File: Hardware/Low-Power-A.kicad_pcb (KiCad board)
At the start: 2 copper layers, 65.4 x 41.3 mm, 27 parts, among them J1 USB_A, J2 01x02, Q1 BC557, Q2 BC547, Q3 BC557, Q4 BC547, Q5 BC547, U1 Arduino_Pro_Micro, U2 VS1838B

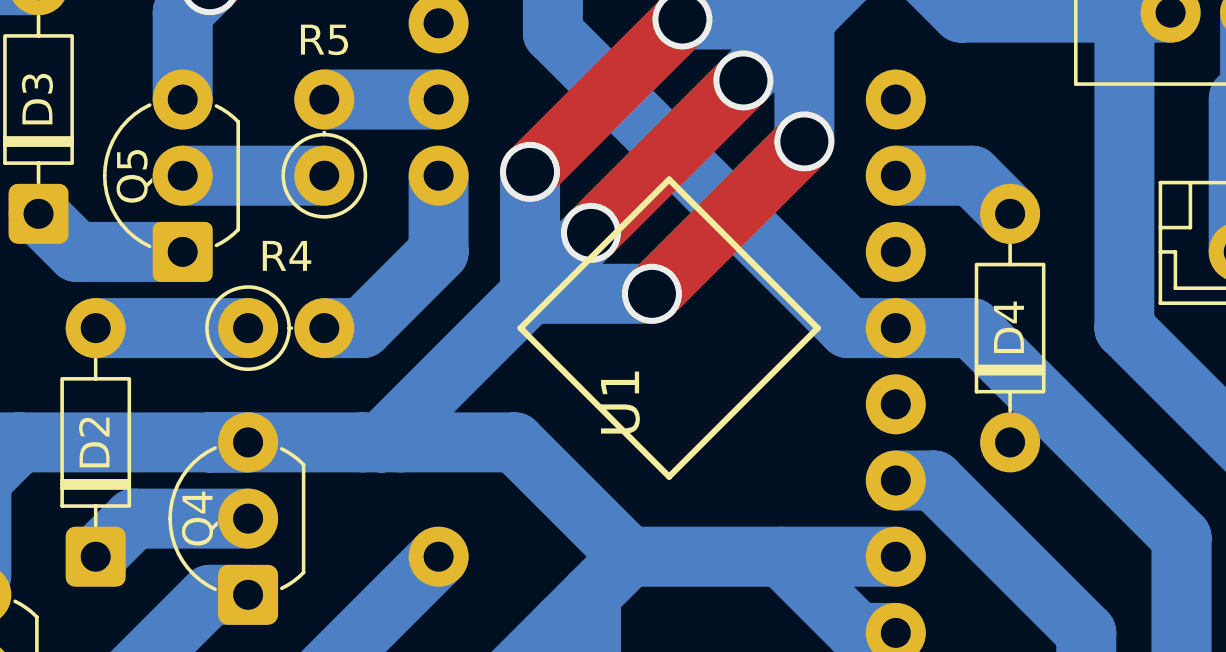
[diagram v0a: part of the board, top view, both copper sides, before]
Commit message: Adding Low-Power-B version schematics & PCB
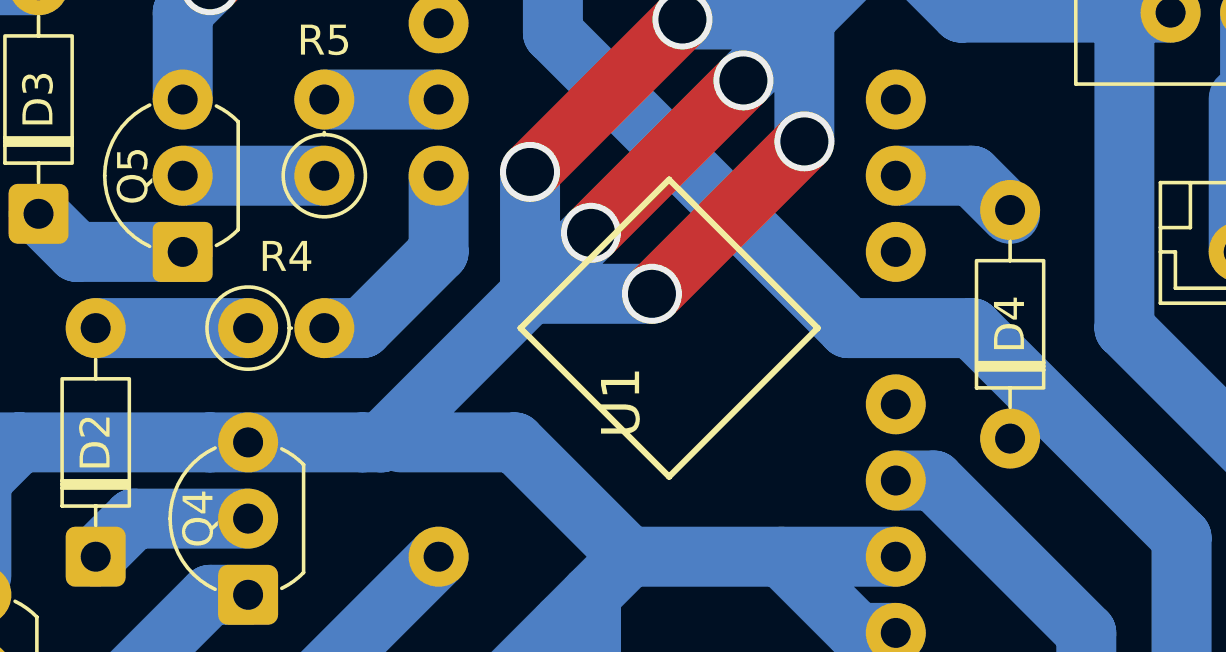
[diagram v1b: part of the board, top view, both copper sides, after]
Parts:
- moved D4 0.13 mm to (161.3, 97.0)
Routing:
- net GND: track 178.4 -> 176.5 mm
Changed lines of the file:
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@@
 	(net 25 "unconnected-(U1-RAW-Pad24)")
 	(net 26 "unconnected-(U1-RX-Pad2)")
-	(net 27 "unconnected-(U1-D4{slash}A6-Pad7)")
 	(footprint "Resistor_THT:R_Axial_DIN0207_L6.3mm_D2.5mm_P2.54mm_Vertical"
 		(layer "F.Cu")
@@
 			(thermal_bridge_angle 0)
 		)
-		(pad "7" thru_hole circle
-			(at -7.62 2.54 180)
-			(size 2 2)
-			(drill 1)
-			(layers "*.Cu" "*.Mask")
-			(remove_unused_layers no)
-			(net 27 "unconnected-(U1-D4{slash}A6-Pad7)")
-			(pinfunction "D4/A6")
-			(pintype "free")
-			(thermal_bridge_angle 0)
-		)
 		(pad "8" thru_hole circle
 			(at -7.62 5.08 180)
@@
 	(footprint "Diode_THT:D_DO-35_SOD27_P7.62mm_Horizontal"
 		(layer "F.Cu")
-		(at 161.29 97.155 90)
+		(at 161.29 97.028 90)
 		(descr "Diode, DO-35_SOD27 series, Axial, Horizontal, pin pitch=7.62mm, length*diameter=4*2mm^2, http://www.diodes.com/_files/packages/DO-35.pdf")
 		(tags "Diode DO-35_SOD27 series Axial Horizontal pin pitch 7.62mm  length 4mm diameter 2mm")
@@
 	)
 	(segment
-		(start 135.89 97.155)
-		(end 134.62 97.155)
-		(width 2)
-		(layer "B.Cu")
-		(net 1)
-	)
-	(segment
 		(start 128.27 97.155)
 		(end 127 97.155)
@@
 		(end 140.97 97.155)
 		(width 2)
-		(layer "B.Cu")
-		(net 1)
-	)
-	(segment
-		(start 140.335 97.155)
-		(end 140.97 97.155)
-		(width 2)
